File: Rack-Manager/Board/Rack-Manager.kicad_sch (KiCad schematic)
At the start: 0 parts

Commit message: Improved some components symbol, also started with schematics design.
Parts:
- added J1: ARJM11C7-114-BA-EW2, Abracon:ARJM11 - Package C, symbol Abracon:ARJM11C7-114-BA-EW2
- added R1: 698R, symbol Device:R_Small_US
- added RV1: 10k, symbol Device:R_Potentiometer_Trim_US
- added U1: Ag9712-FL, Silvertel:Ag9700, symbol Silvertel:Ag9712-FL
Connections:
- new net: R1.1, U1.5 (CP_{[1]})
- new net: R1.2, U1.6 (CP_{[2]})
- new net: RV1.2, U1.9 (ADJ)
- new net: J1.1 (VC_{[2]}-), U1.4 (V_{B2})
- new net: J1.2 (VC_{[1]}-), U1.2 (V_{A1})
- new net: J1.6 (VC_{[2]}+), U1.3 (V_{B1})
- new net: J1.7 (VC_{[1]}+), U1.1 (V_{A1})
- new net 12V_PoE: RV1.3, U1.8 (V_{DC}+)
- new net Earth: J1.15 (MH_{[1]}), J1.16 (MH_{[2]})
- new net GND: RV1.1, U1.7 (V_{DC}-)

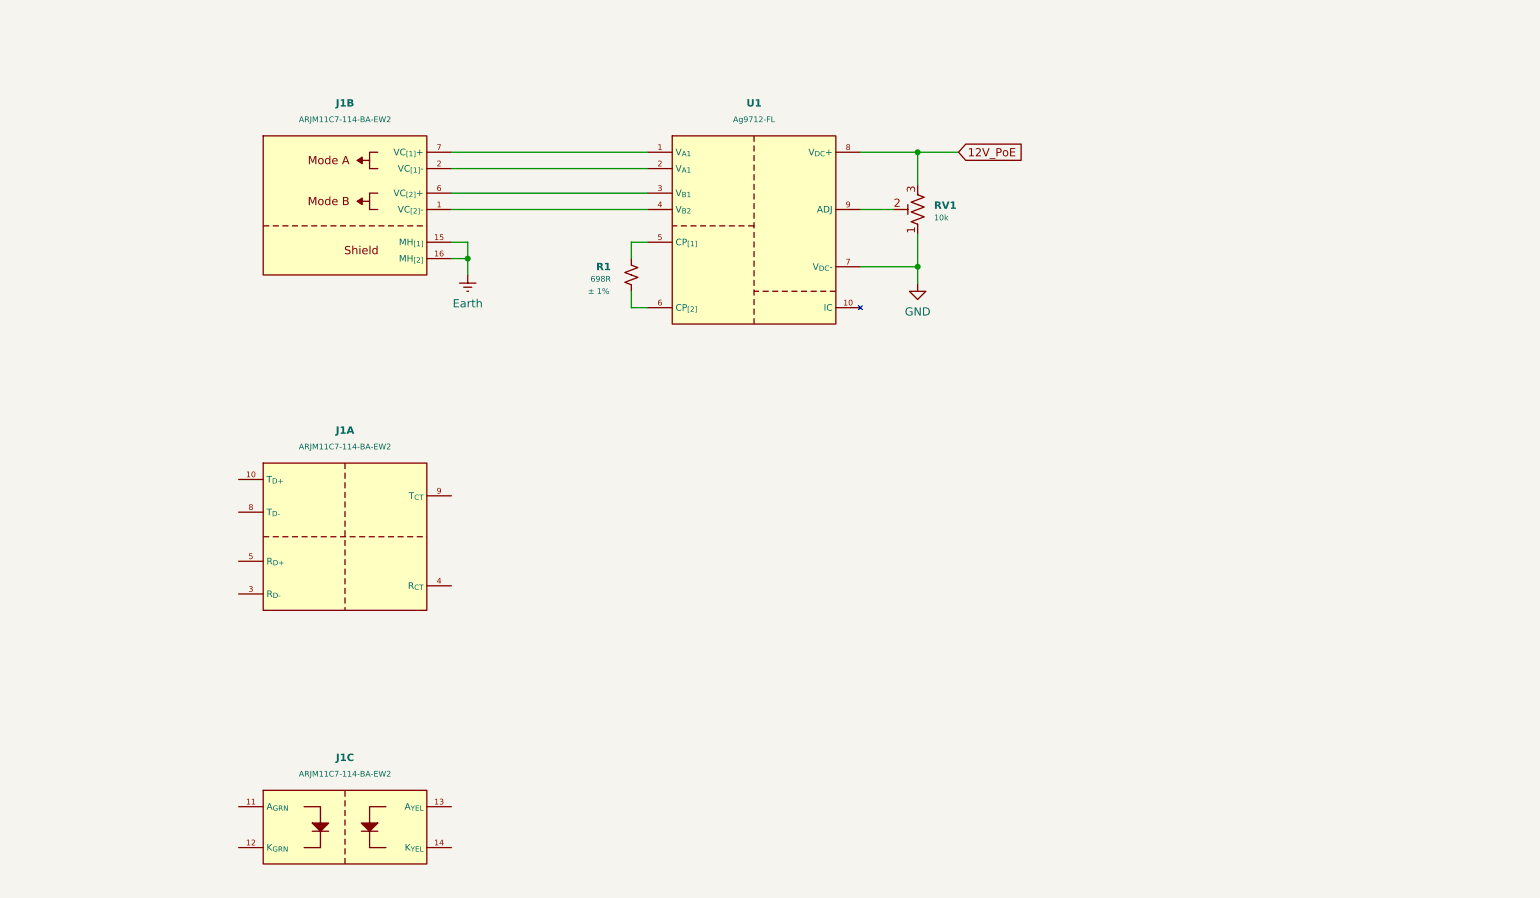
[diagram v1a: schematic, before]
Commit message: Added USB-PD power circuit to the schematics.
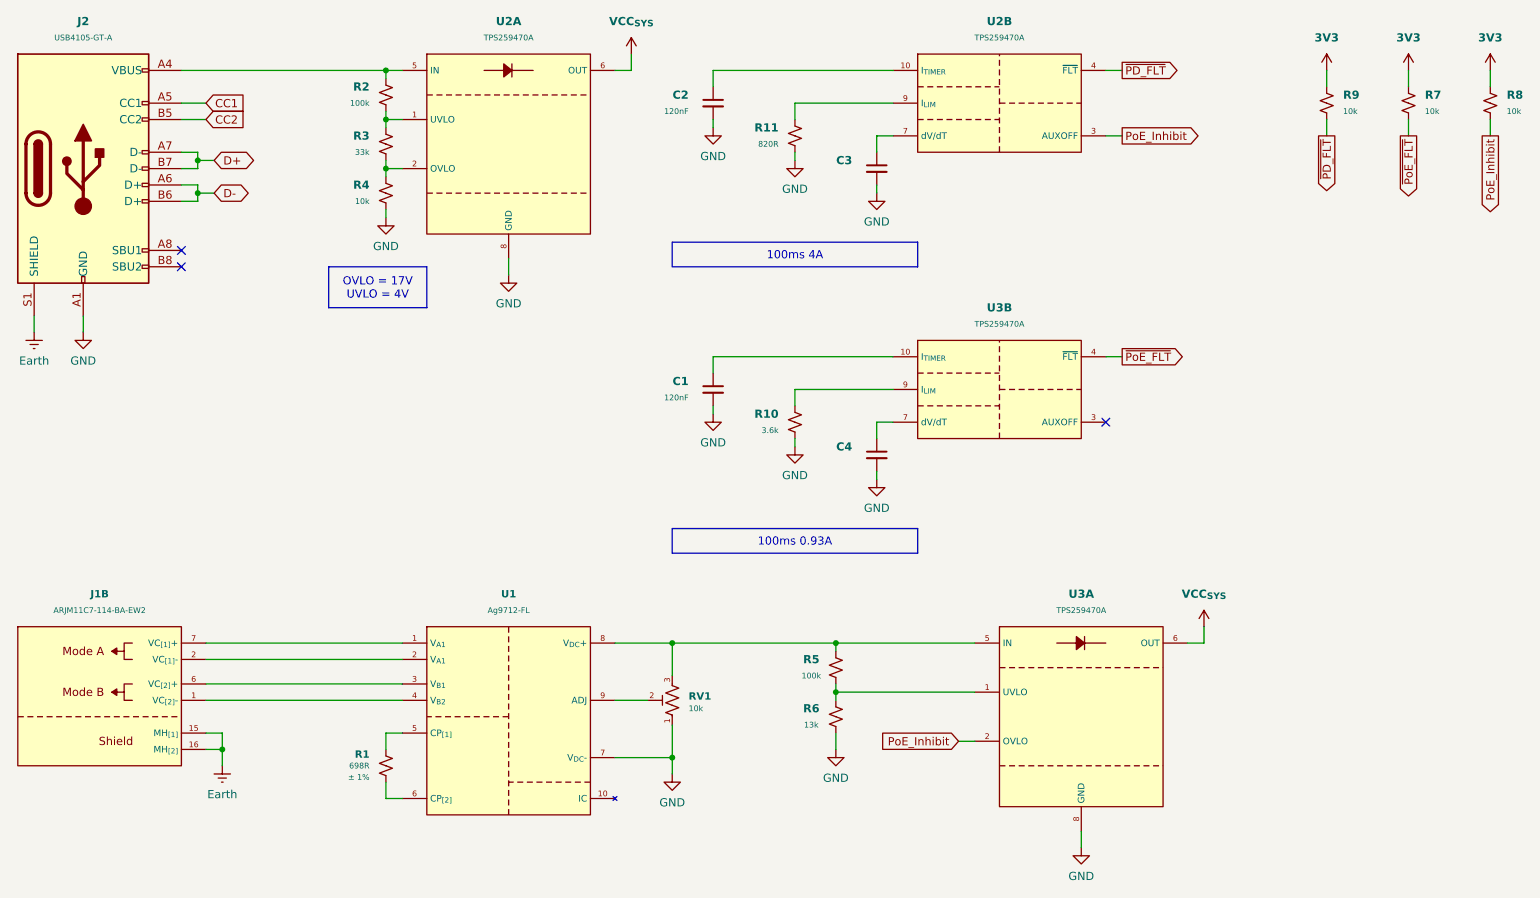
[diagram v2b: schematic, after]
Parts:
- removed unit 1 of J1
- removed unit 3 of J1
- added C1, C2: 120nF, Capacitor_SMD:C_0402_1005Metric, symbol Device:C_Small
- added C3, C4: ~, Capacitor_SMD:C_0402_1005Metric, symbol Device:C_Small
- added J2: USB4105-GT-A, Connector_USB:USB_C_Receptacle_GCT_USB4105-xx-A_16P_TopMnt_Horizontal, symbol Connector:USB_C_Receptacle_USB2.0_16P
- added R10: 3.6k, symbol Device:R_Small_US
- added R11: 820R, symbol Device:R_Small_US
- added R2, R5: 100k, symbol Device:R_Small_US
- added R3: 33k, symbol Device:R_Small_US
- added R4, R7, R8, R9: 10k, symbol Device:R_Small_US
- added R6: 13k, symbol Device:R_Small_US
- added U2, U3: TPS259470A, Texas Instruments:RPW0010A, symbol Texas Instruments:TPS259470A
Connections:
- net Earth: now also J2.S1 (SHIELD)
- net GND: now also C1.2, C2.2, C3.2, C4.2, J2.A1 (GND), J2.A12 (GND), J2.B1 (GND), J2.B12 (GND), R10.2, R11.2, R4.2, R6.1, U2.8 (GND), U3.8 (GND)
- net 12V_PoE: no longer names the net of RV1.3, U1.8 (V_{DC}+)
- net 12V_PoE: now also R5.1, U3.5 (IN)
- new net: C1.1, U3.10 (I_{TIMER})
- new net: J2.A4 (VBUS), J2.A9 (VBUS), J2.B4 (VBUS), J2.B9 (VBUS), R2.1, U2.5 (IN)
- new net: R2.2, R3.1, U2.1 (ENABLE)
- new net: C3.1, U2.7 (dV/dT)
- new net: R3.2, R4.1, U2.2 (OVLO)
- new net: R5.2, R6.2, U3.1 (ENABLE)
- new net: C2.1, U2.10 (I_{TIMER})
- new net: R10.1, U3.9 (I_{LIM})
- new net: R11.1, U2.9 (I_{LIM})
- new net: C4.1, U3.7 (dV/dT)
- new net 3V3: R7.1, R8.1, R9.1
- new net CC1: J2.A5 (CC1)
- new net CC2: J2.B5 (CC2)
- new net D+: J2.A7 (D-), J2.B7 (D-)
- new net D-: J2.A6 (D+), J2.B6 (D+)
- new net PoE_Inhibit: R8.2, U2.3 (AUXOFF), U3.2 (OVLO)
- new net VCC_{SYS}: U2.6 (OUT), U3.6 (OUT)
- new net ~{PD_FLT}: R9.2, U2.4 (~{FLT})
- new net ~{PoE_FLT}: R7.2, U3.4 (~{FLT})
- no-connect marks 0 -> 3
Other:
- moved on the sheet: J1B, R1, RV1, U1

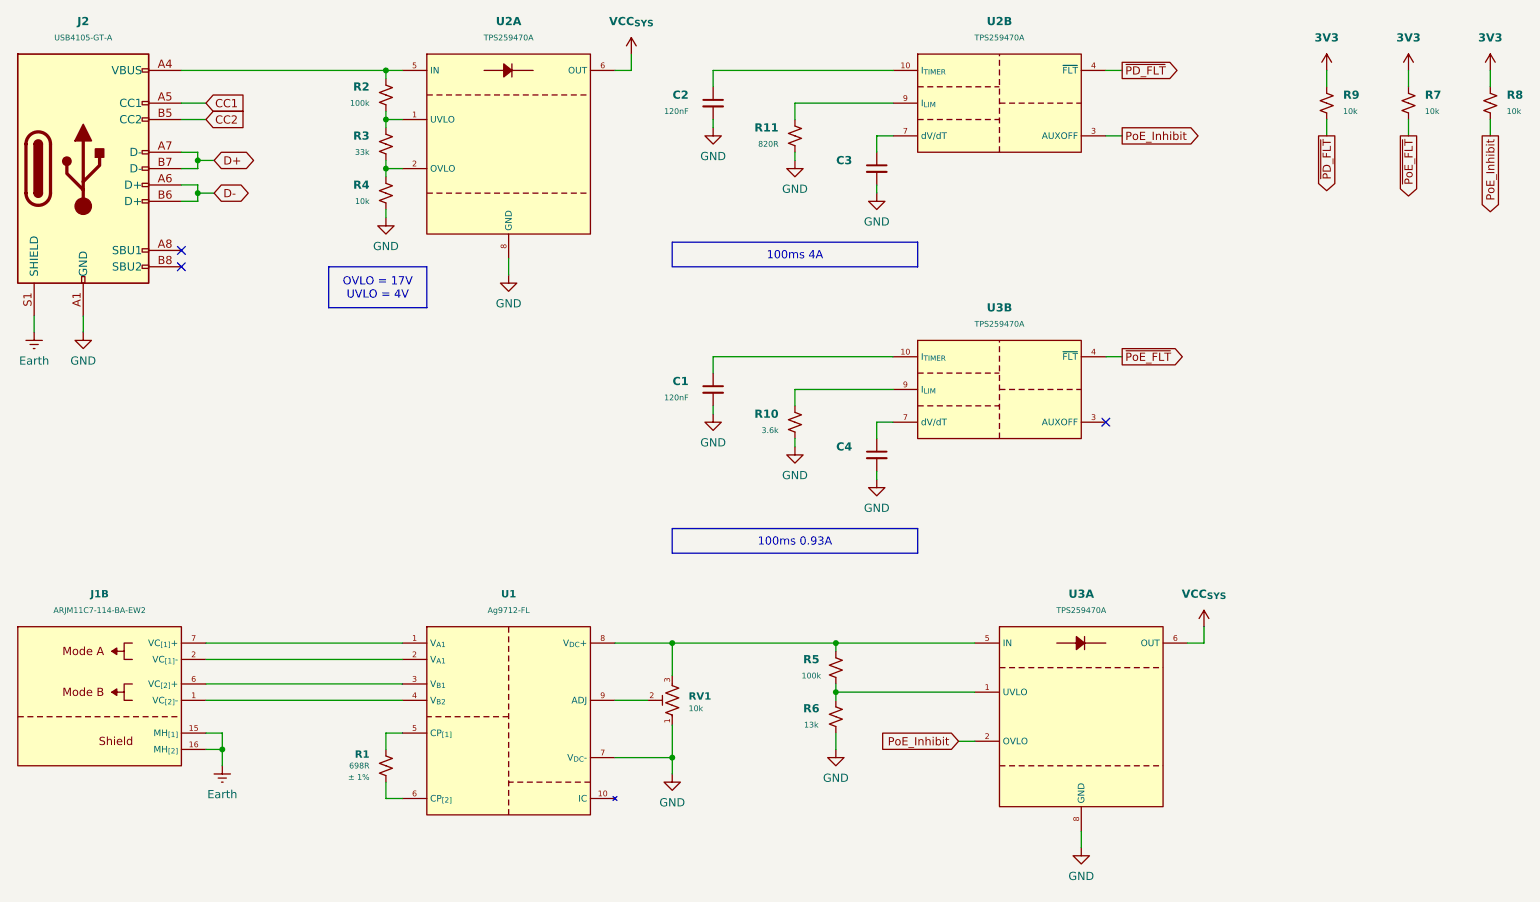
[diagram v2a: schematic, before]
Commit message: Updated Silvertel and Texas Instruments KiCAD libraries. Continued with the schematics design.
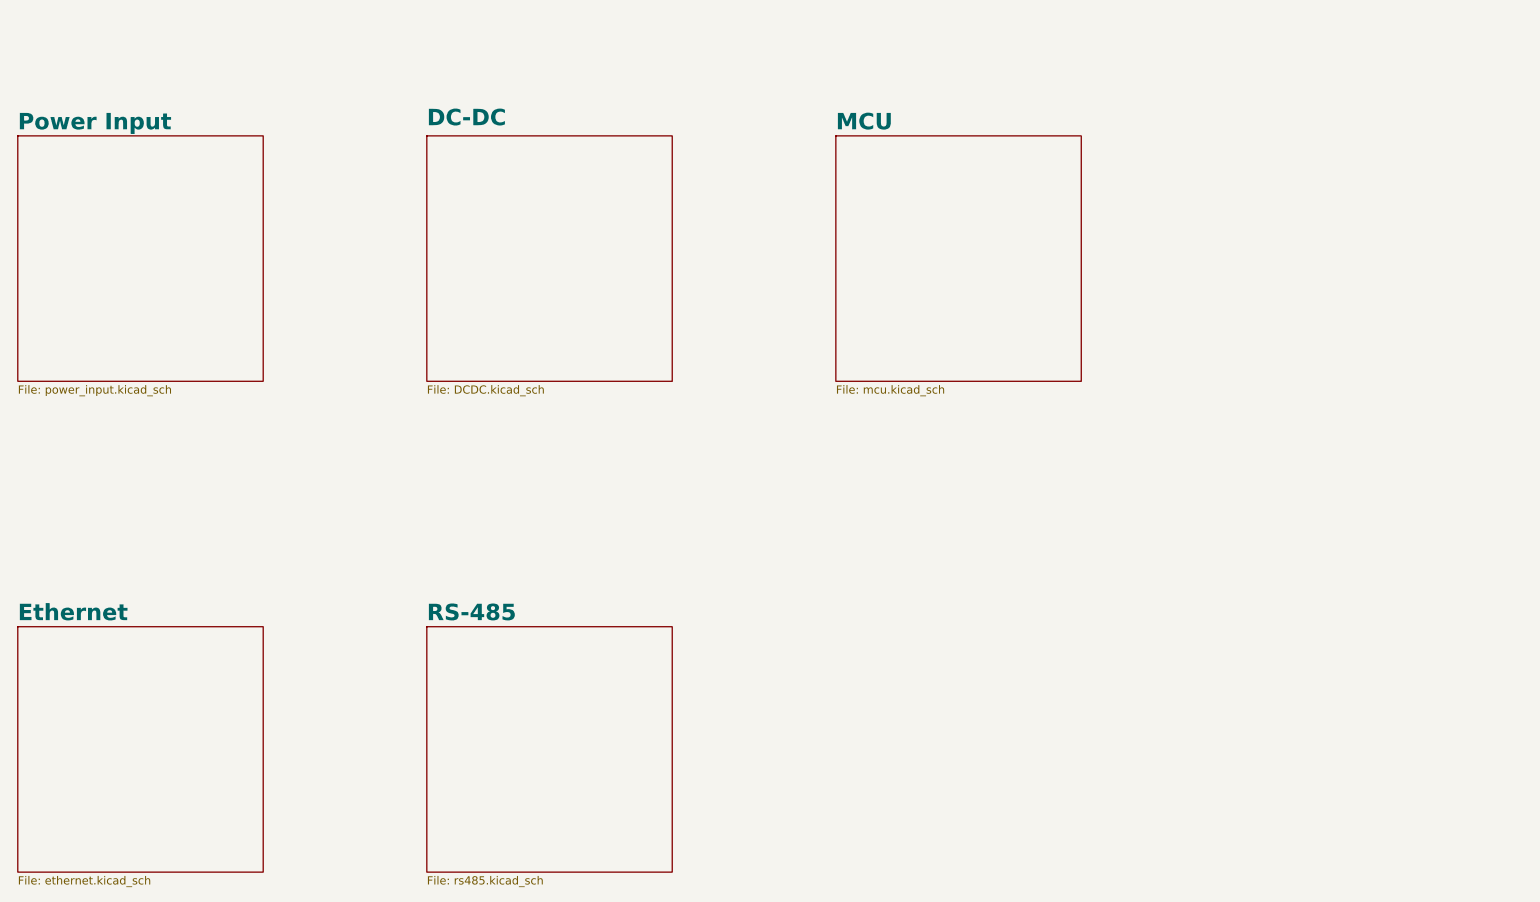
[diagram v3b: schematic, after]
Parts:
- removed C1, C2: 120nF, Capacitor_SMD:C_0402_1005Metric, symbol Device:C_Small
- removed C3, C4: ~, Capacitor_SMD:C_0402_1005Metric, symbol Device:C_Small
- removed J1: ARJM11C7-114-BA-EW2, Abracon:ARJM11 - Package C, symbol Abracon:ARJM11C7-114-BA-EW2
- removed J2: USB4105-GT-A, Connector_USB:USB_C_Receptacle_GCT_USB4105-xx-A_16P_TopMnt_Horizontal, symbol Connector:USB_C_Receptacle_USB2.0_16P
- removed R1: 698R, symbol Device:R_Small_US
- removed R10: 3.6k, symbol Device:R_Small_US
- removed R11: 820R, symbol Device:R_Small_US
- removed R2, R5: 100k, symbol Device:R_Small_US
- removed R3: 33k, symbol Device:R_Small_US
- removed R4, R7, R8, R9: 10k, symbol Device:R_Small_US
- removed R6: 13k, symbol Device:R_Small_US
- removed RV1: 10k, symbol Device:R_Potentiometer_Trim_US
- removed U1: Ag9712-FL, Silvertel:Ag9700, symbol Silvertel:Ag9712-FL
- removed U2, U3: TPS259470A, Texas Instruments:RPW0010A, symbol Texas Instruments:TPS259470A
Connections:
- no-connect marks 3 -> 0
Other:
- added sheet DC-DC (DCDC.kicad_sch)
- added sheet Ethernet (ethernet.kicad_sch)
- added sheet MCU (mcu.kicad_sch)
- added sheet Power Input (power_input.kicad_sch)
- added sheet RS-485 (rs485.kicad_sch)

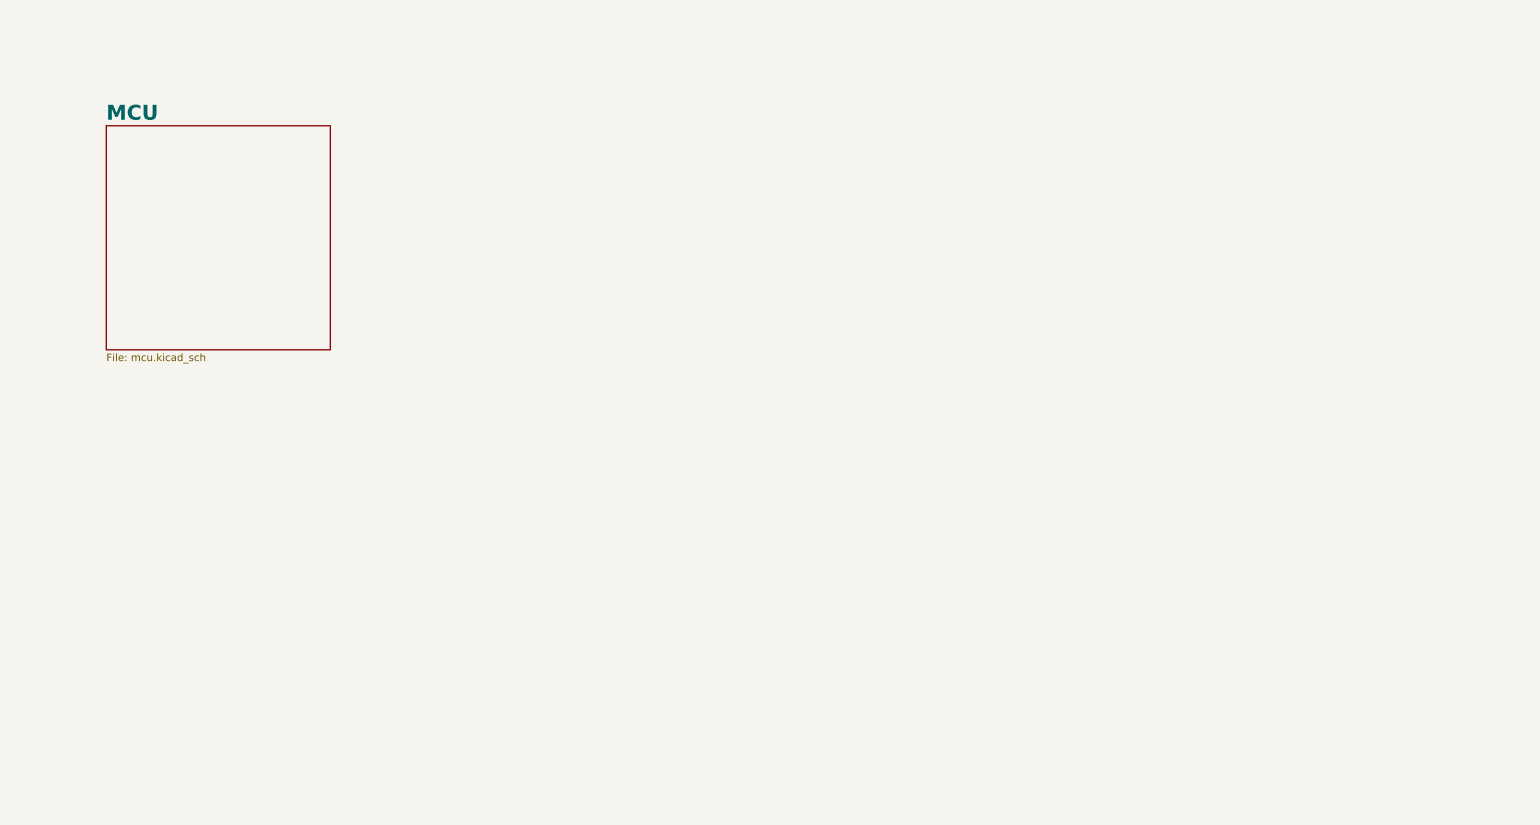
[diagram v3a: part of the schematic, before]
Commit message: Added Bourns library, updated Texas Instruments library, continued with schematic drawing.
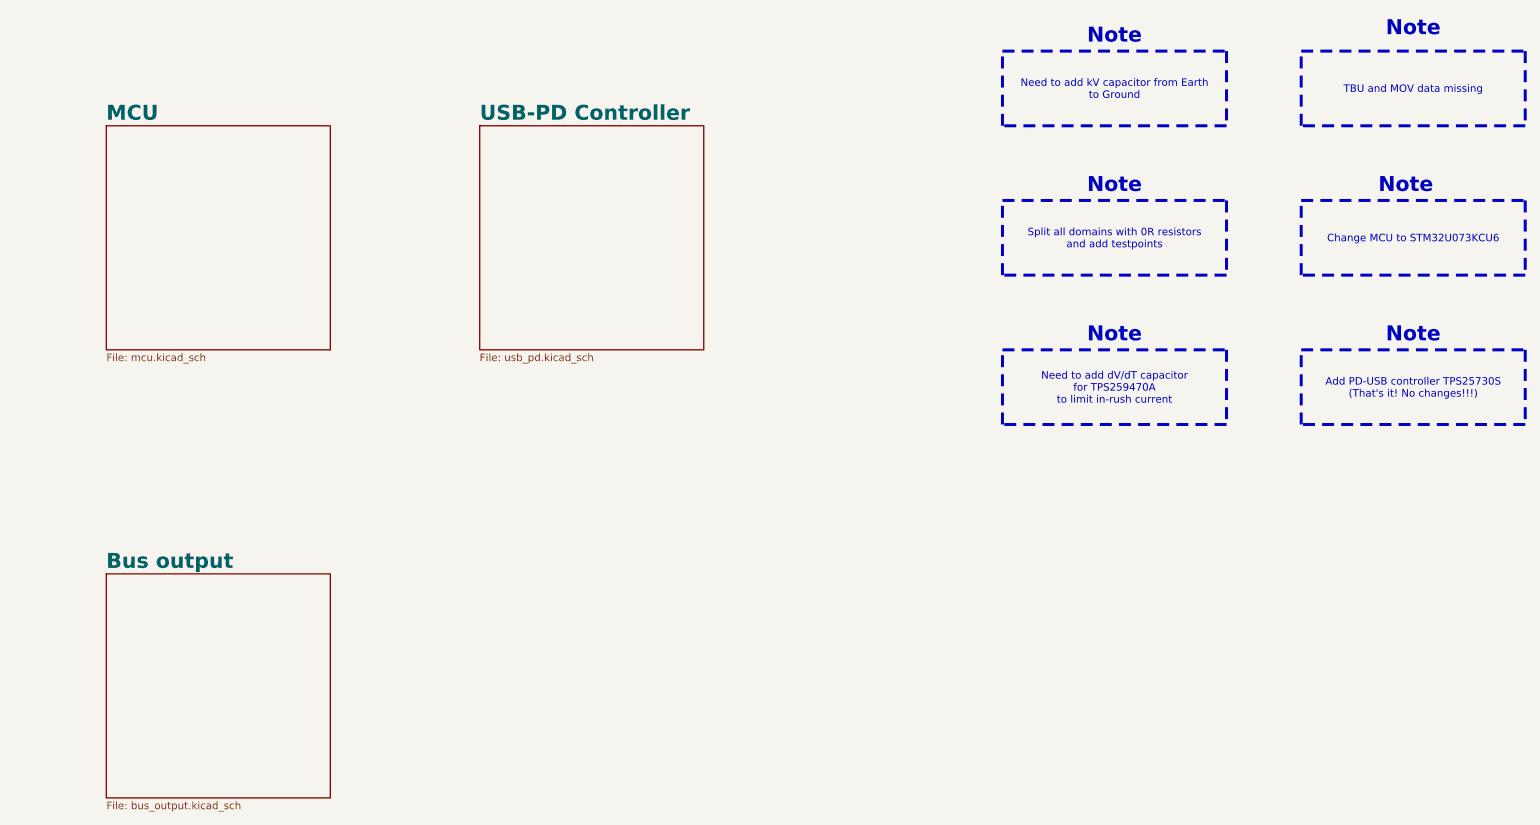
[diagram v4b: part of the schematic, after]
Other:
- added sheet Bus output (bus_output.kicad_sch)
- added sheet USB-PD Controller (usb_pd.kicad_sch)
- note added: "Note"
- title: (none) -> Index
